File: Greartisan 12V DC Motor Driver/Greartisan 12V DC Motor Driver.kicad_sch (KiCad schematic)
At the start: 7 parts, among them M1 Motor_DC, M2 Motor_DC, U1 L298N, U2 LM7812_TO220

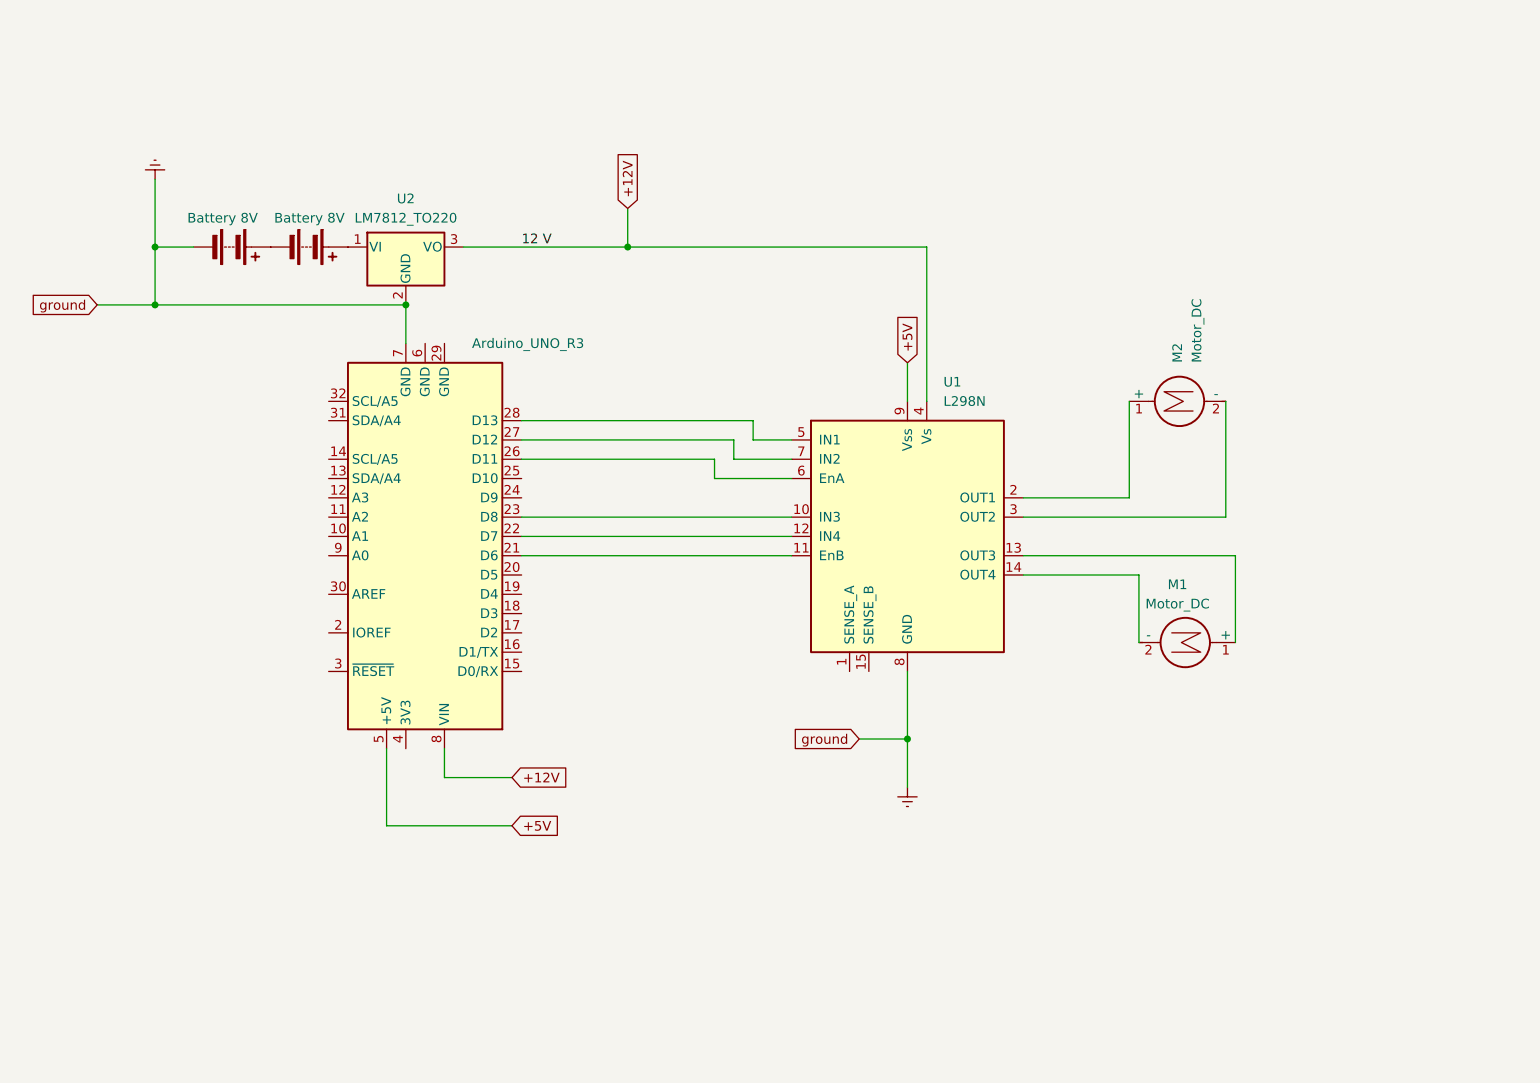
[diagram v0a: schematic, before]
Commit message: update voltage regulators:
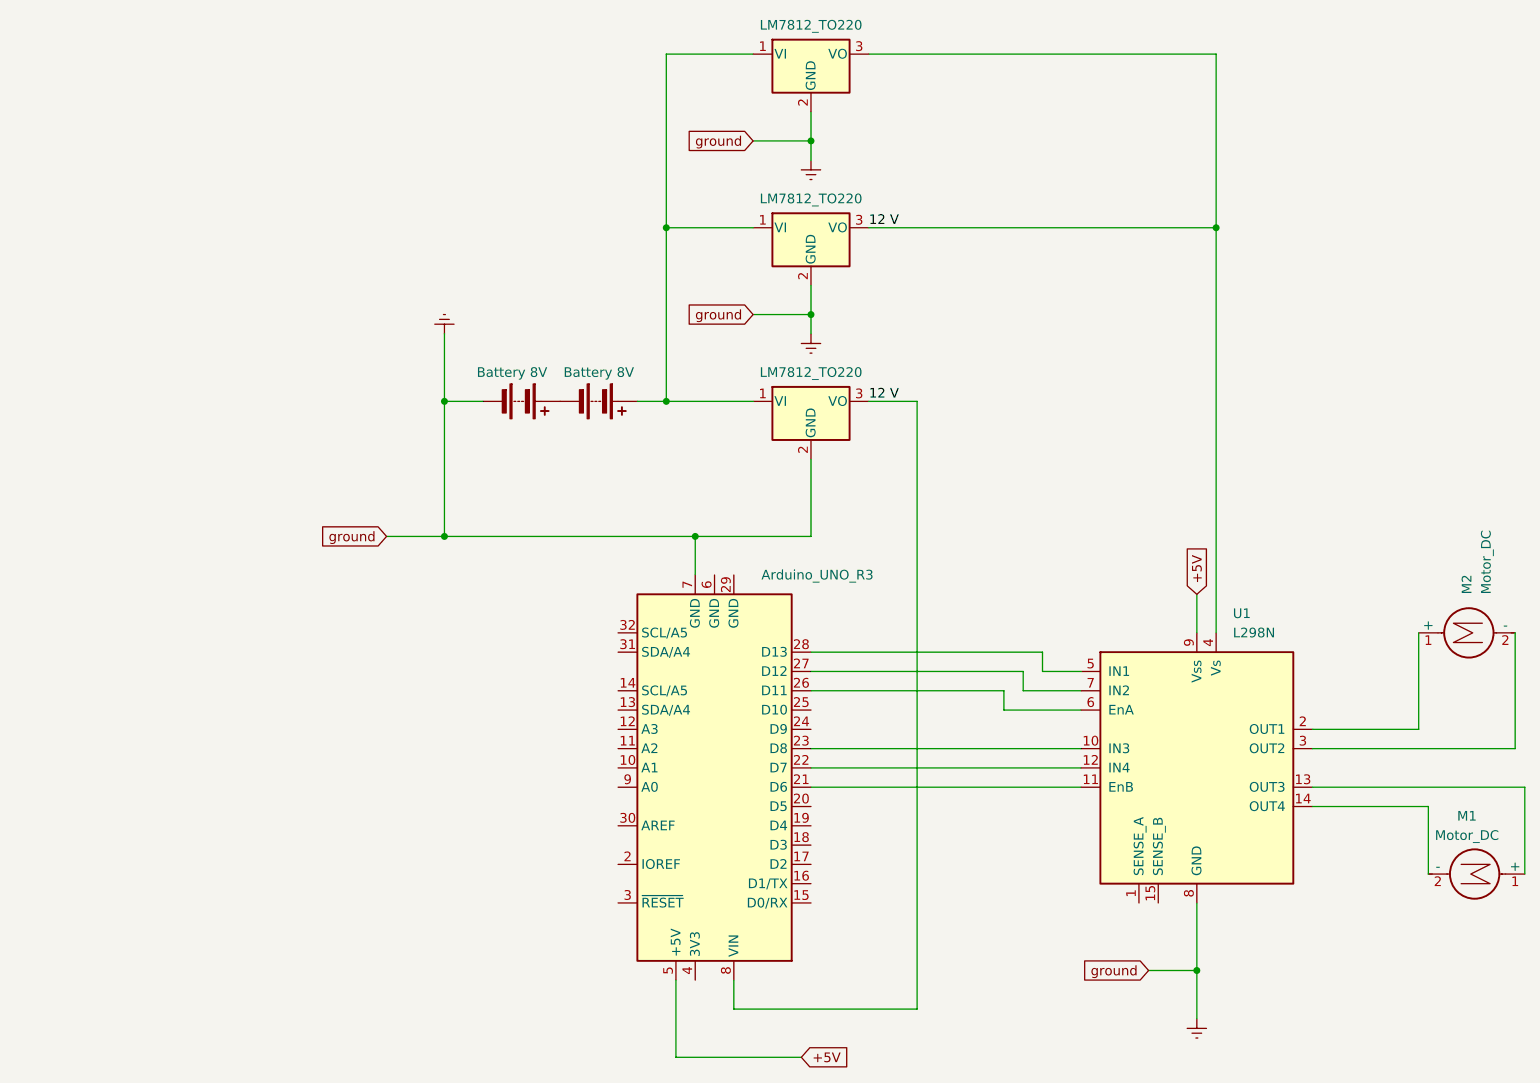
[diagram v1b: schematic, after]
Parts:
- added U3, U4: LM7812_TO220, Package_TO_SOT_THT:TO-220-3_Vertical, symbol Regulator_Linear:LM7812_TO220
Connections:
- net Earth: now also U3.2 (GND), U4.2 (GND)
- net at BT2.1 (+), U2.1 (VI): now also U3.1 (VI), U4.1 (VI)
- net +12V renamed 12 V
- net 12 V: now also U3.3 (VO), U4.3 (VO)
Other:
- moved on the sheet: M1, M2, U1
